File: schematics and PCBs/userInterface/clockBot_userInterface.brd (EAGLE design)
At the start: 67.3 x 32.7 mm, 6 parts, among them X1 5566-8

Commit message: User interface PCB update
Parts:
- moved VOLUME 52.0 mm to (109.7, 6.18)
- moved FILTER_CUTOFF 46.2 mm to (85.8, 6.18)
- moved S1 17.0 mm to (37.2, 7.01), turned to 270 degrees
- moved X1 16.2 mm to (59.3, 6.29)
- moved OCTAVE_SELECT 14.1 mm to (10.6, 6.26)
- moved R1 7.83 mm to (24.3, 7.71)
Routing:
- net N$5: track 59.0 -> 104.8 mm
- net N$4: track 42.1 -> 77.2 mm
- net N$10: track 26.0 -> 55.4 mm
- net N$6: track 24.5 -> 53.9 mm
- net N$1: track 58.5 -> 35.1 mm
- net N$3: track 17.7 -> 33.1 mm
- net N$8: track 47.4 -> 59.1 mm
- net N$2: track 13.3 -> 24.8 mm
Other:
- board size 67.3 x 32.7 mm -> 119.6 x 14.6 mm

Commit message: Fixed switch on user interface
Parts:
- removed S1: (no value), adafruit:B3F-31XX
- added SW1: SPST_TACT-EVQQ2, adafruit:EVQ-Q2
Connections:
- net 0: now also SW1.A; no longer S1.1
- net N$1: now also SW1.B; no longer S1.2
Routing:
- net N$1: track 35.1 -> 37.1 mm, vias 0 -> 1
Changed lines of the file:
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@@
 <attribute name="VALUE" x="22.475396875" y="3.6615375" size="1.27" layer="27" ratio="10"/>
-</element>
-<element name="S1" library="adafruit" library_urn="urn:adsk.eagle:library:420" package="B3F-31XX" package3d_urn="urn:adsk.eagle:package:6240698/1" value="" x="37.236203125" y="7.014421875" smashed="yes" rot="R270">
-<attribute name="NAME" x="39.776203125" y="8.284421875" size="1.27" layer="25" ratio="10" rot="R270"/>
-<attribute name="VALUE" x="31.267203125" y="10.697421875" size="1.27" layer="27" ratio="10" rot="R270"/>
 </element>
 <element name="VOLUME" library="pot" library_urn="urn:adsk.eagle:library:331" package="S64W" package3d_urn="urn:adsk.eagle:package:22708/1" value="10K Ohms" x="109.73866875" y="6.176921875" smashed="yes">
@@
 <attribute name="POPULARITY" value="0" x="84.71755625" y="-1.328471875" size="1.778" layer="27" display="off"/>
 <attribute name="VALUE" x="56.77755625" y="13.276528125" size="1.27" layer="27"/>
+</element>
+<element name="SW1" library="adafruit" library_urn="urn:adsk.eagle:library:420" package="EVQ-Q2" package3d_urn="urn:adsk.eagle:package:6240643/1" value="SPST_TACT-EVQQ2" x="38.618578125" y="6.69720625" smashed="yes">
+<attribute name="NAME" x="35.618578125" y="10.19720625" size="1.27" layer="25"/>
+<attribute name="VALUE" x="35.418578125" y="1.89720625" size="1.27" layer="27"/>
 </element>
 </elements>
@@
 <signal name="N$1">
 <contactref element="R1" pad="2"/>
-<contactref element="S1" pad="2"/>
 <contactref element="X1" pad="6"/>
 <wire x1="33.2232" y1="7.62" x2="29.5656" y2="7.62" width="0.1524" layer="16"/>
-<wire x1="35.9664" y1="4.8768" x2="33.2232" y2="7.62" width="0.1524" layer="16"/>
+<wire x1="35.9664" y1="4.8768" x2="33.6804" y2="7.1628" width="0.1524" layer="16"/>
+<wire x1="33.6804" y1="7.1628" x2="33.2232" y2="7.62" width="0.1524" layer="16"/>
 <wire x1="29.5656" y1="7.62" x2="29.415996875" y2="7.7065375" width="0.1524" layer="16"/>
-<wire x1="35.9664" y1="4.8768" x2="35.991603125" y2="4.753821875" width="0.1524" layer="16"/>
 <wire x1="59.7408" y1="8.9916" x2="61.4172" y2="8.9916" width="0.1524" layer="16"/>
 <wire x1="55.7784" y1="5.0292" x2="59.7408" y2="8.9916" width="0.1524" layer="16"/>
@@
 <wire x1="36.1188" y1="4.8768" x2="36.2712" y2="5.0292" width="0.1524" layer="16"/>
 <wire x1="61.4172" y1="8.9916" x2="61.41755625" y2="9.041528125" width="0.1524" layer="16"/>
-<wire x1="36.1188" y1="4.8768" x2="35.991603125" y2="4.753821875" width="0.1524" layer="16"/>
+<contactref element="SW1" pad="B"/>
+<wire x1="33.6804" y1="7.1628" x2="35.2044" y2="8.6868" width="0.1524" layer="1"/>
+<wire x1="35.2044" y1="8.6868" x2="35.218578125" y2="8.69720625" width="0.1524" layer="1"/>
+<wire x1="36.1188" y1="4.8768" x2="35.9664" y2="4.8768" width="0.1524" layer="16"/>
+<via x="33.6804" y="7.1628" extent="1-16" drill="0.35"/>
 </signal>
 <signal name="N$5">
@@
 <contactref element="R1" pad="1"/>
 </signal>
-<signal name="0">
-<contactref element="S1" pad="1"/>
-</signal>
 <signal name="N$6">
 <contactref element="VOLUME" pad="A"/>
@@
 <wire x1="61.5696" y1="3.6576" x2="61.41755625" y2="3.541528125" width="0.1524" layer="16"/>
 </signal>
+<signal name="0">
+<contactref element="SW1" pad="A"/>
+</signal>
 </signals>

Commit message: User itnerface switch update
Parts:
- removed SW1: SPST_TACT-EVQQ2, adafruit:EVQ-Q2
- added S1: (no value), switch-omron:B3F-10XX
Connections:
- net 0: now also S1.3; no longer SW1.A
- net N$1: now also S1.1; no longer SW1.B
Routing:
- net N$1: track 37.1 -> 40.4 mm
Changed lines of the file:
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@@
 <attribute name="VALUE" x="56.77755625" y="13.276528125" size="1.27" layer="27"/>
 </element>
-<element name="SW1" library="adafruit" library_urn="urn:adsk.eagle:library:420" package="EVQ-Q2" package3d_urn="urn:adsk.eagle:package:6240643/1" value="SPST_TACT-EVQQ2" x="38.618578125" y="6.69720625" smashed="yes">
-<attribute name="NAME" x="35.618578125" y="10.19720625" size="1.27" layer="25"/>
-<attribute name="VALUE" x="35.418578125" y="1.89720625" size="1.27" layer="27"/>
+<element name="S1" library="switch-omron" library_urn="urn:adsk.eagle:library:377" package="B3F-10XX" package3d_urn="urn:adsk.eagle:package:27496/1" value="" x="40.585625" y="8.88335625" smashed="yes">
+<attribute name="MF" value="" x="40.585625" y="8.88335625" size="1.778" layer="27" display="off"/>
+<attribute name="MPN" value="B3F-1000" x="40.585625" y="8.88335625" size="1.778" layer="27" display="off"/>
+<attribute name="NAME" x="37.537625" y="12.56635625" size="1.27" layer="25" ratio="10"/>
+<attribute name="OC_FARNELL" value="176432" x="40.585625" y="8.88335625" size="1.778" layer="27" display="off"/>
+<attribute name="OC_NEWARK" value="36M3542" x="40.585625" y="8.88335625" size="1.778" layer="27" display="off"/>
+<attribute name="POPULARITY" value="72" x="40.585625" y="8.88335625" size="1.778" layer="27" display="off"/>
+<attribute name="VALUE" x="37.537625" y="3.80335625" size="1.27" layer="27" ratio="10"/>
 </element>
 </elements>
@@
 <wire x1="57.3024" y1="9.144" x2="57.21755625" y2="9.041528125" width="0.1524" layer="16"/>
 <wire x1="17.9832" y1="7.4676" x2="13.1064" y2="7.4676" width="0.1524" layer="1"/>
-<wire x1="19.5072" y1="5.9436" x2="17.9832" y2="7.4676" width="0.1524" layer="1"/>
-<wire x1="54.102" y1="5.9436" x2="19.5072" y2="5.9436" width="0.1524" layer="1"/>
-<wire x1="57.15" y1="8.9916" x2="54.102" y2="5.9436" width="0.1524" layer="1"/>
+<wire x1="19.76740625" y1="5.68339375" x2="17.9832" y2="7.4676" width="0.1524" layer="1"/>
+<wire x1="53.84179375" y1="5.68339375" x2="19.76740625" y2="5.68339375" width="0.1524" layer="1"/>
+<wire x1="57.15" y1="8.9916" x2="53.84179375" y2="5.68339375" width="0.1524" layer="1"/>
 <wire x1="13.1064" y1="7.4676" x2="13.10555625" y2="7.5334625" width="0.1524" layer="1"/>
 <wire x1="57.15" y1="8.9916" x2="57.21755625" y2="9.041528125" width="0.1524" layer="1"/>
@@
 <contactref element="X1" pad="6"/>
 <wire x1="33.2232" y1="7.62" x2="29.5656" y2="7.62" width="0.1524" layer="16"/>
-<wire x1="35.9664" y1="4.8768" x2="33.6804" y2="7.1628" width="0.1524" layer="16"/>
-<wire x1="33.6804" y1="7.1628" x2="33.2232" y2="7.62" width="0.1524" layer="16"/>
+<wire x1="35.9236875" y1="4.8768" x2="33.6804" y2="7.1200875" width="0.1524" layer="16"/>
+<wire x1="33.6804" y1="7.1200875" x2="33.6804" y2="7.1628" width="0.1524" layer="16"/>
+<wire x1="33.6804" y1="7.1628" x2="33.3756" y2="7.4676" width="0.1524" layer="16"/>
+<wire x1="33.3756" y1="7.4676" x2="33.2232" y2="7.62" width="0.1524" layer="16"/>
 <wire x1="29.5656" y1="7.62" x2="29.415996875" y2="7.7065375" width="0.1524" layer="16"/>
 <wire x1="59.7408" y1="8.9916" x2="61.4172" y2="8.9916" width="0.1524" layer="16"/>
@@
 <wire x1="36.1188" y1="4.8768" x2="36.2712" y2="5.0292" width="0.1524" layer="16"/>
 <wire x1="61.4172" y1="8.9916" x2="61.41755625" y2="9.041528125" width="0.1524" layer="16"/>
-<contactref element="SW1" pad="B"/>
-<wire x1="33.6804" y1="7.1628" x2="35.2044" y2="8.6868" width="0.1524" layer="1"/>
-<wire x1="35.2044" y1="8.6868" x2="35.218578125" y2="8.69720625" width="0.1524" layer="1"/>
-<wire x1="36.1188" y1="4.8768" x2="35.9664" y2="4.8768" width="0.1524" layer="16"/>
+<wire x1="36.1188" y1="4.8768" x2="35.9236875" y2="4.8768" width="0.1524" layer="16"/>
 <via x="33.6804" y="7.1628" extent="1-16" drill="0.35"/>
+<contactref element="S1" pad="1"/>
+<wire x1="33.528" y1="7.4676" x2="37.1856" y2="11.1252" width="0.1524" layer="16"/>
+<wire x1="33.3756" y1="7.4676" x2="33.528" y2="7.4676" width="0.1524" layer="16"/>
+<wire x1="37.1856" y1="11.1252" x2="37.334425" y2="11.14395625" width="0.1524" layer="16"/>
 </signal>
 <signal name="N$5">
@@
 </signal>
 <signal name="0">
-<contactref element="SW1" pad="A"/>
+<contactref element="S1" pad="3"/>
 </signal>
 </signals>

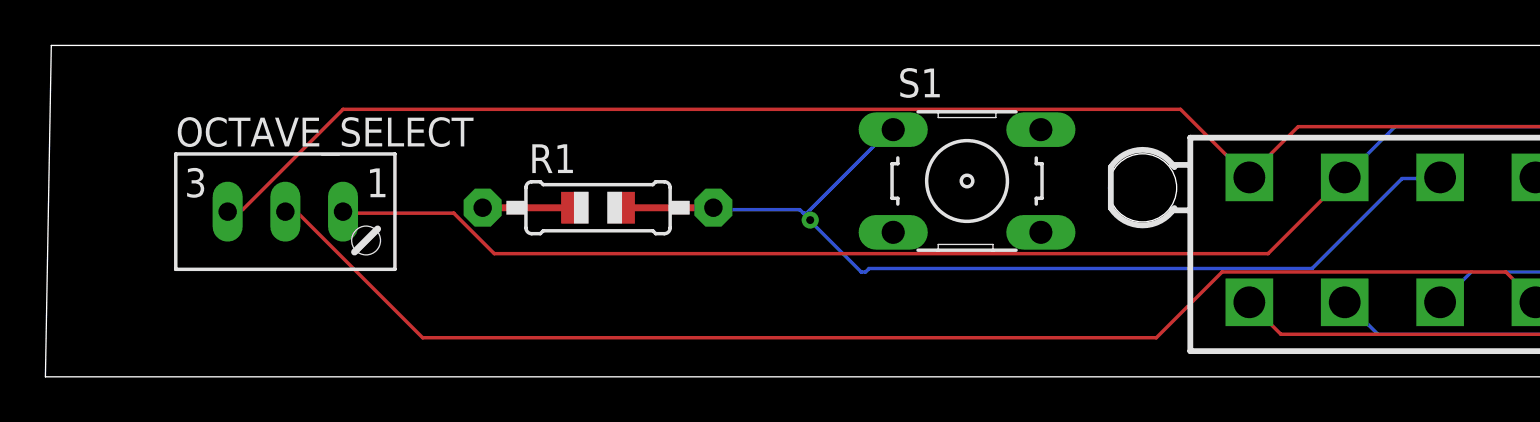
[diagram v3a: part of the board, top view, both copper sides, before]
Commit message: User itnerface switch update
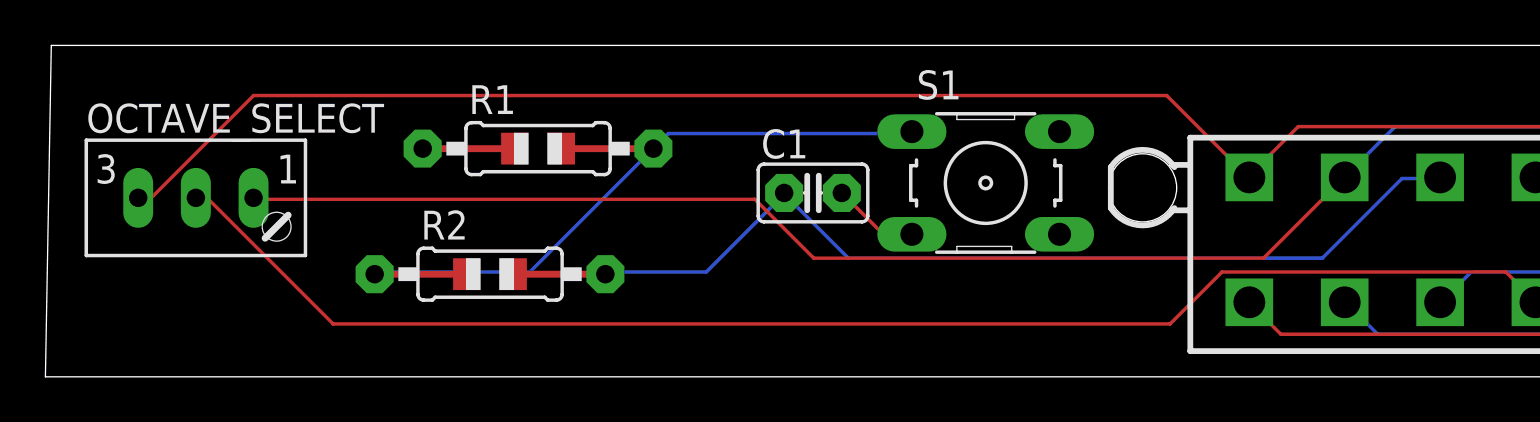
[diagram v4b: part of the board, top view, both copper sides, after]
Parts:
- added C1: 50 nF, adafruit:C025-025X050
- added R2: 10K Ohms, adafruit:0805-THM
- R1: value 10K Ohms -> 100K Ohms
- moved OCTAVE_SELECT 3.99 mm to (6.63, 6.87)
- moved R1 3.71 mm to (21.7, 10.3)
- moved S1 0.83 mm to (41.4, 8.80)
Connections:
- new net N$7: R1.2, R2.1, S1.1
- net 0: now also C1.2
- net N$1: now also C1.1, R2.2; no longer R1.2, S1.1
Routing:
- net N$7: track 0.00 -> 26.3 mm
- net N$4: track 77.4 -> 81.7 mm
- net N$5: track 104.8 -> 109.0 mm
- net 0: track 0.00 -> 3.83 mm
- net N$8: track 59.1 -> 62.8 mm
- net N$1: track 40.4 -> 41.0 mm, vias 1 -> 0

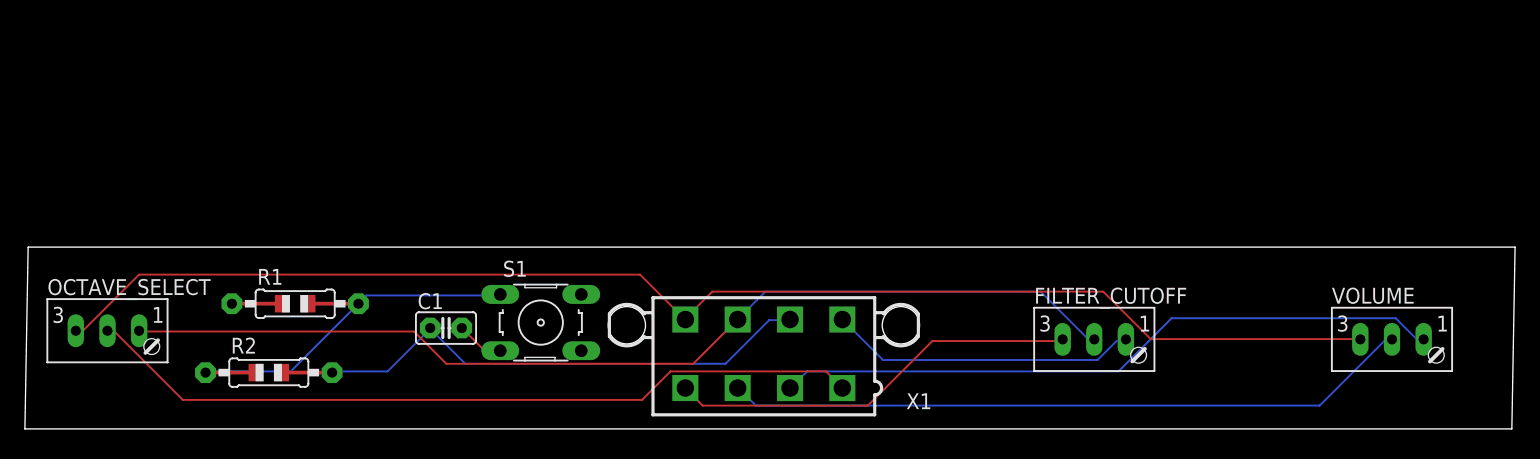
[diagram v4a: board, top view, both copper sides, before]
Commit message: User interface single row molex
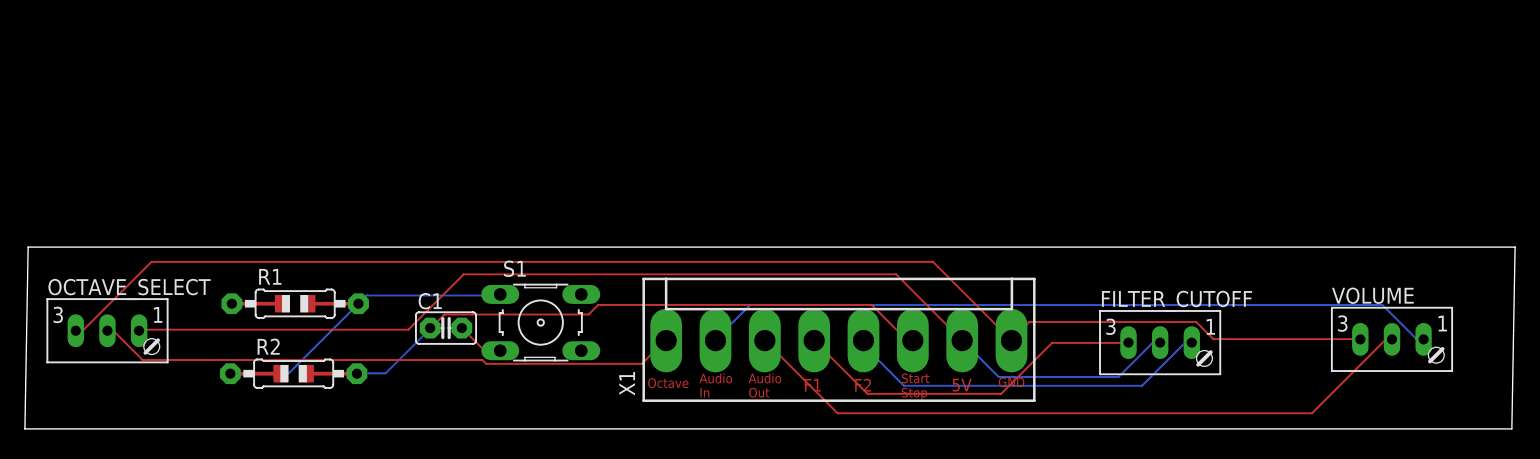
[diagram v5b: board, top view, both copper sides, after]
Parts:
- X1: value 5566-8 -> (none); device con-molex:5566-8 -> con-molex:KK-156-8
- moved X1 6.11 mm to (65.3, 7.35)
- moved FILTER_CUTOFF 5.29 mm to (91.1, 5.92)
- moved R2 2.00 mm to (21.6, 4.69)
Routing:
- net N$8: track 62.8 -> 46.7 mm
- net N$1: track 41.0 -> 48.1 mm
- net N$4: track 81.7 -> 88.4 mm
- net N$6: track 53.9 -> 59.2 mm
- net N$2: track 24.8 -> 29.5 mm
- net N$3: track 33.1 -> 28.7 mm
- net N$7: track 26.3 -> 24.3 mm
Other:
- board text added: "5V"
- board text added: "Audio In"
- board text added: "Audio Out"
- board text added: "F1"
- board text added: "F2"
- board text added: "GND"
- board text added: "Octave"
- board text added: "Start Stop"
